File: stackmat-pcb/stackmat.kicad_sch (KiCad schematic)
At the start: 14 parts, among them U2 18650, U3 AMS1117-3.3

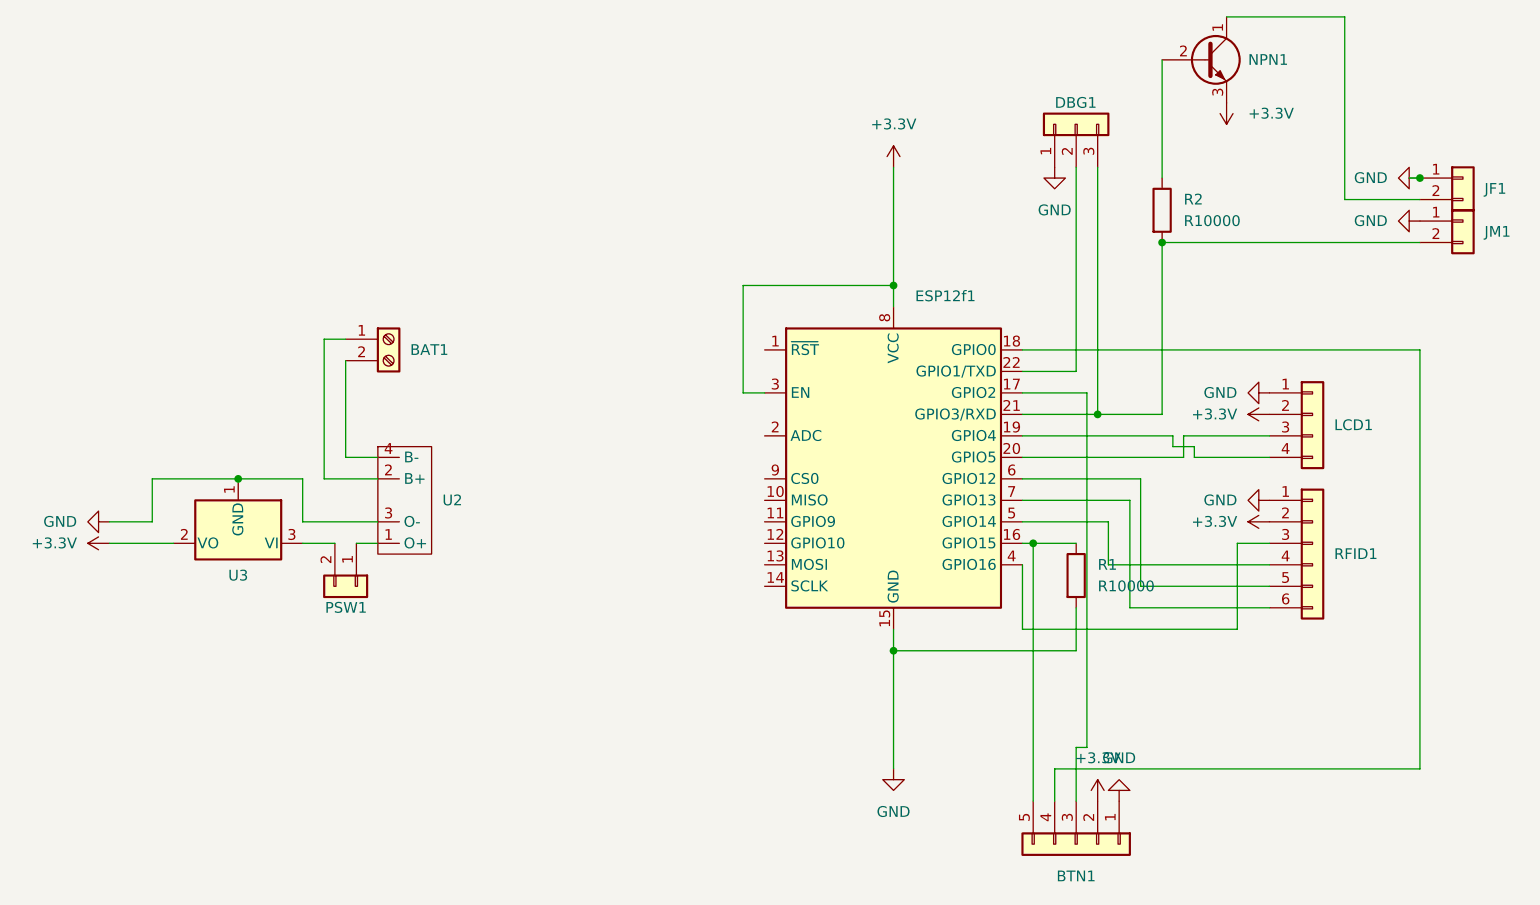
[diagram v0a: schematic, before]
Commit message: fix: lcd 5v instead of 3.3v
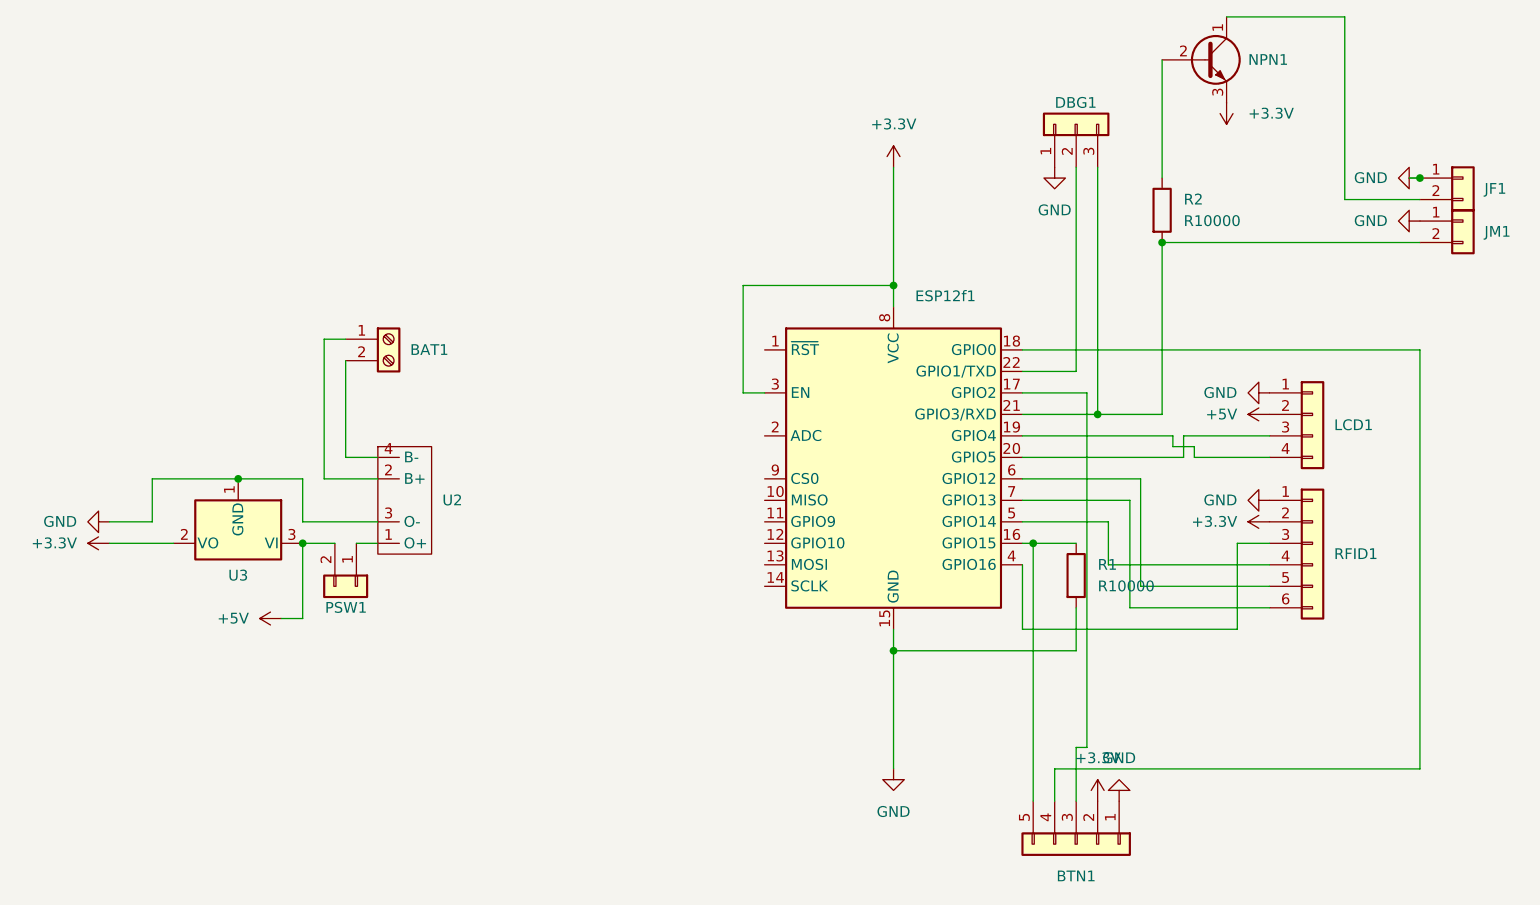
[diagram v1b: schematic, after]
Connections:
- net +3.3V: no longer LCD1.2 (Pin_2)
- net +5V: now reaches PSW1.2 (Pin_2), U3.3 (VI)
- net +5V: now also LCD1.2 (Pin_2)
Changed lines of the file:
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@@
   (junction (at 140.97 68.58) (diameter 0) (color 0 0 0 0)
   )
+  (junction (at 71.12 99.06) (diameter 0) (color 0 0 0 0)
+  )
   (junction (at 157.48 99.06) (diameter 0) (color 0 0 0 0)
   )
@@
     (stroke (width 0) (type default))
   )
+  (wire (pts (xy 68.58 107.95) (xy 71.12 107.95))
+    (stroke (width 0) (type default))
+  )
   (wire (pts (xy 48.26 96.52) (xy 53.34 96.52))
     (stroke (width 0) (type default))
@@
   )
   (wire (pts (xy 71.12 91.44) (xy 63.5 91.44))
+    (stroke (width 0) (type default))
+  )
+  (wire (pts (xy 71.12 99.06) (xy 71.12 107.95))
     (stroke (width 0) (type default))
   )
@@
         (path "/ccd0dcac-df1d-4089-8f7e-e62a3e2f6f2a"
           (reference "BTN1") (unit 1)
+        )
+      )
+    )
+  )
+  (symbol (lib_id "power:+5V") (at 185.42 83.82 90) (unit 1)
+    (in_bom yes) (on_board yes) (dnp no) (fields_autoplaced)
+    (property "Reference" "#PWR04" (at 189.23 83.82 0)
+      (effects (font (size 1.27 1.27)) hide)
+    )
+    (property "Value" "+5V" (at 181.61 83.82 90)
+      (effects (font (size 1.27 1.27)) (justify left))
+    )
+    (property "Footprint" "" (at 185.42 83.82 0)
+      (effects (font (size 1.27 1.27)) hide)
+    )
+    (property "Datasheet" "" (at 185.42 83.82 0)
+      (effects (font (size 1.27 1.27)) hide)
+    )
+    (pin "1")
+    (instances
+      (project "stackmat"
+        (path "/ccd0dcac-df1d-4089-8f7e-e62a3e2f6f2a"
+          (reference "#PWR04") (unit 1)
         )
       )
@@
     )
   )
-  (symbol (lib_id "power:+3.3V") (at 185.42 83.82 90) (unit 1)
-    (in_bom yes) (on_board yes) (dnp no) (fields_autoplaced)
-    (property "Reference" "#PWR0105" (at 189.23 83.82 0)
-      (effects (font (size 1.27 1.27)) hide)
-    )
-    (property "Value" "+3.3V" (at 181.61 83.8199 90)
-      (effects (font (size 1.27 1.27)) (justify left))
-    )
-    (property "Footprint" "" (at 185.42 83.82 0)
-      (effects (font (size 1.27 1.27)) hide)
-    )
-    (property "Datasheet" "" (at 185.42 83.82 0)
-      (effects (font (size 1.27 1.27)) hide)
-    )
-    (pin "1")
-    (instances
-      (project "stackmat"
-        (path "/ccd0dcac-df1d-4089-8f7e-e62a3e2f6f2a"
-          (reference "#PWR0105") (unit 1)
-        )
-      )
-    )
-  )
   (symbol (lib_id "power:GND") (at 160.02 54.61 0) (unit 1)
     (in_bom yes) (on_board yes) (dnp no) (fields_autoplaced)
@@
         )
       )
+    )
+  )
+  (symbol (lib_id "power:+5V") (at 68.58 107.95 90) (unit 1)
+    (in_bom yes) (on_board yes) (dnp no) (fields_autoplaced)
+    (property "Reference" "#PWR03" (at 72.39 107.95 0)
+      (effects (font (size 1.27 1.27)) hide)
+    )
+    (property "Value" "+5V" (at 64.77 107.95 90)
+      (effects (font (size 1.27 1.27)) (justify left))
+    )
+    (property "Footprint" "" (at 68.58 107.95 0)
+      (effects (font (size 1.27 1.27)) hide)
+    )
+    (property "Datasheet" "" (at 68.58 107.95 0)
+      (effects (font (size 1.27 1.27)) hide)
+    )
+    (pin "1")
+    (instances
+      (project "stackmat"
+        (path "/ccd0dcac-df1d-4089-8f7e-e62a3e2f6f2a"
+          (reference "#PWR03") (unit 1)
+        )
+      )

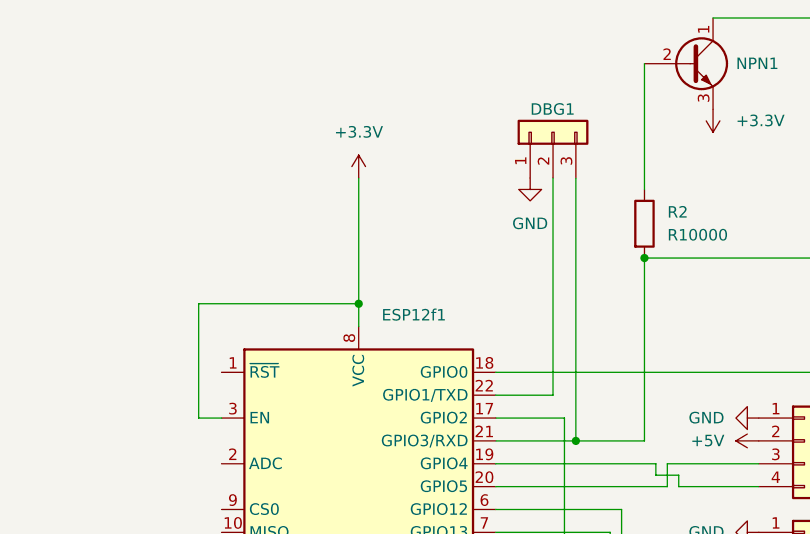
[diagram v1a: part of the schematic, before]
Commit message: feat: better pcb debug pins
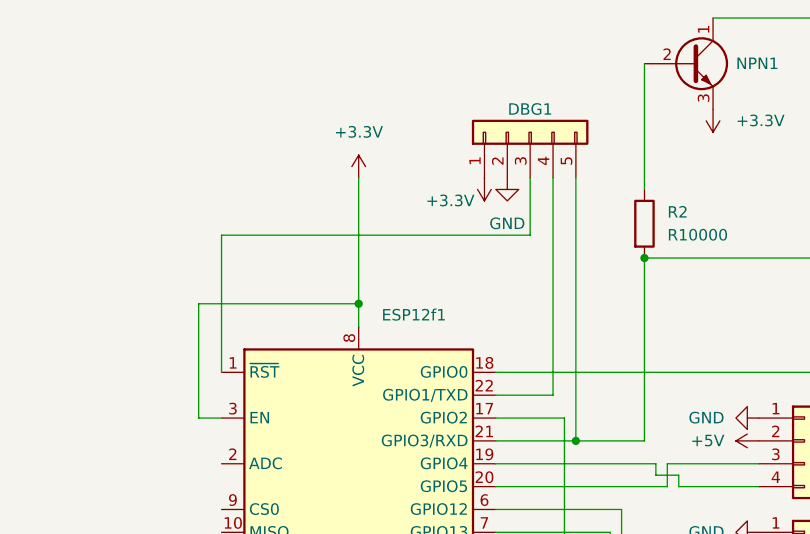
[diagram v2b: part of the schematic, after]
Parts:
- removed DBG1: DBG_SERIAL, Connector_PinHeader_2.00mm:PinHeader_1x03_P2.00mm_Vertical, symbol Connector_Generic:Conn_01x03
- added DBG1: Conn_01x05, Connector_PinHeader_2.54mm:PinHeader_1x05_P2.54mm_Vertical, symbol Connector_Generic:Conn_01x05
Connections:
- net +3.3V: now also DBG1.1 (Pin_1)
- net GND: now also DBG1.2 (Pin_2)
- net at ESP12f1.1 (~{RST}): now also DBG1.3 (Pin_3)
- net at ESP12f1.21 (GPIO3/RXD), JM1.2 (Pin_2), R2.2: now also DBG1.5 (Pin_5)
- net at ESP12f1.22 (GPIO1/TXD): now also DBG1.4 (Pin_4)
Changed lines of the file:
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@@
+    (stroke (width 0) (type default))
+  )
+  (wire (pts (xy 125.73 76.2) (xy 125.73 60.96))
     (stroke (width 0) (type default))
   )
@@
     (stroke (width 0) (type default))
   )
+  (wire (pts (xy 125.73 60.96) (xy 160.02 60.96))
+    (stroke (width 0) (type default))
+  )
   (wire (pts (xy 162.56 123.19) (xy 162.56 129.54))
     (stroke (width 0) (type default))
@@
   )
   (wire (pts (xy 170.18 91.44) (xy 156.21 91.44))
+    (stroke (width 0) (type default))
+  )
+  (wire (pts (xy 160.02 54.61) (xy 160.02 60.96))
     (stroke (width 0) (type default))
   )
@@
         (path "/ccd0dcac-df1d-4089-8f7e-e62a3e2f6f2a"
           (reference "PSW1") (unit 1)
+        )
+      )
+    )
+  )
+  (symbol (lib_id "Connector_Generic:Conn_01x05") (at 160.02 49.53 90) (unit 1)
+    (in_bom yes) (on_board yes) (dnp no)
+    (property "Reference" "DBG1" (at 160.02 46.99 90)
+      (effects (font (size 1.27 1.27)))
+    )
+    (property "Value" "Conn_01x05" (at 160.02 45.72 90)
+      (effects (font (size 1.27 1.27)) hide)
+    )
+    (property "Footprint" "Connector_PinHeader_2.54mm:PinHeader_1x05_P2.54mm_Vertical" (at 160.02 49.53 0)
+      (effects (font (size 1.27 1.27)) hide)
+    )
+    (property "Datasheet" "~" (at 160.02 49.53 0)
+      (effects (font (size 1.27 1.27)) hide)
+    )
+    (pin "1")
+    (pin "3")
+    (pin "2")
+    (pin "5")
+    (pin "4")
+    (instances
+      (project "stackmat"
+        (path "/ccd0dcac-df1d-4089-8f7e-e62a3e2f6f2a"
+          (reference "DBG1") (unit 1)
         )
       )
@@
     )
   )
-  (symbol (lib_id "power:GND") (at 160.02 54.61 0) (unit 1)
-    (in_bom yes) (on_board yes) (dnp no) (fields_autoplaced)
-    (property "Reference" "#PWR0102" (at 160.02 60.96 0)
-      (effects (font (size 1.27 1.27)) hide)
-    )
-    (property "Value" "GND" (at 160.02 59.69 0)
+  (symbol (lib_id "power:GND") (at 157.48 54.61 0) (unit 1)
+    (in_bom yes) (on_board yes) (dnp no) (fields_autoplaced)
+    (property "Reference" "#PWR0102" (at 157.48 60.96 0)
+      (effects (font (size 1.27 1.27)) hide)
+    )
+    (property "Value" "GND" (at 157.48 59.69 0)
       (effects (font (size 1.27 1.27)))
     )
-    (property "Footprint" "" (at 160.02 54.61 0)
-      (effects (font (size 1.27 1.27)) hide)
-    )
-    (property "Datasheet" "" (at 160.02 54.61 0)
+    (property "Footprint" "" (at 157.48 54.61 0)
+      (effects (font (size 1.27 1.27)) hide)
+    )
+    (property "Datasheet" "" (at 157.48 54.61 0)
       (effects (font (size 1.27 1.27)) hide)
     )
@@
         (path "/ccd0dcac-df1d-4089-8f7e-e62a3e2f6f2a"
           (reference "#PWR0107") (unit 1)
-        )
-      )
-    )
-  )
-  (symbol (lib_id "Connector_Generic:Conn_01x03") (at 162.56 49.53 90) (unit 1)
-    (in_bom yes) (on_board yes) (dnp no)
-    (property "Reference" "DBG1" (at 160.02 46.99 90)
-      (effects (font (size 1.27 1.27)) (justify right))
-    )
-    (property "Value" "DBG_SERIAL" (at 167.64 50.7999 90)
-      (effects (font (size 1.27 1.27)) (justify right) hide)
-    )
-    (property "Footprint" "Connector_PinHeader_2.00mm:PinHeader_1x03_P2.00mm_Vertical" (at 162.56 49.53 0)
-      (effects (font (size 1.27 1.27)) hide)
-    )
-    (property "Datasheet" "~" (at 162.56 49.53 0)
-      (effects (font (size 1.27 1.27)) hide)
-    )
-    (pin "1")
-    (pin "2")
-    (pin "3")
-    (instances
-      (project "stackmat"
-        (path "/ccd0dcac-df1d-4089-8f7e-e62a3e2f6f2a"
-          (reference "DBG1") (unit 1)
         )
       )
@@
         )
       )
+    )
+  )
+  (symbol (lib_id "power:+3.3V") (at 154.94 54.61 180) (unit 1)
+    (in_bom yes) (on_board yes) (dnp no)
+    (property "Reference" "#PWR05" (at 154.94 50.8 0)
+      (effects (font (size 1.27 1.27)) hide)
+    )
+    (property "Value" "+3.3V" (at 151.13 57.15 0)
+      (effects (font (size 1.27 1.27)))
+    )
+    (property "Footprint" "" (at 154.94 54.61 0)
+      (effects (font (size 1.27 1.27)) hide)
+    )
+    (property "Datasheet" "" (at 154.94 54.61 0)
+      (effects (font (size 1.27 1.27)) hide)
+    )
+    (pin "1")
+    (instances
+      (project "stackmat"
+        (path "/ccd0dcac-df1d-4089-8f7e-e62a3e2f6f2a"
+          (reference "#PWR05") (unit 1)
+        )
+      )
